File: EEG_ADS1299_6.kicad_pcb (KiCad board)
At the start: 2 copper layers, 49.6 x 21.2 mm, 90 parts, among them IC1 ADS1299, P1 CONN_2, P2 CONN_2, P3 CONN_1, P4 CONN_1, P5 CONN_01X08, P6 CONN_2, U1 TPS2294x, U2 TPS61222, U3 NRF528XX-QFAA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

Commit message: Final version, v4.
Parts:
- removed P5: CONN_01X08, Pin_Headers:Pin_Header_Straight_2x04_Pitch2.54mm
- added P10: CONN_01X02, Pin_Headers:Pin_Header_Straight_1x02_Pitch2.54mm, F.Cu at (311.0, 129.1)
- added P7: CONN_01X02, Pin_Headers:Pin_Header_Straight_1x02_Pitch2.54mm, F.Cu at (308.6, 116.0)
- added P8: CONN_01X02, Pin_Headers:Pin_Header_Straight_1x02_Pitch2.54mm, F.Cu at (311.0, 118.7)
- added P9: CONN_01X02, Pin_Headers:Pin_Header_Straight_1x02_Pitch2.54mm, F.Cu at (311.0, 123.9)
- moved P6 22.5 mm to (291.0, 116.6), turned to 90 degrees
- moved D1 17.4 mm to (273.0, 131.2)
- moved C3 16.2 mm to (270.3, 115.1), turned to 270 degrees (x2)
- moved C37 15.4 mm to (289.3, 119.0), turned to 90 degrees
- moved D2 15.3 mm to (274.2, 131.2)
- moved R14 15.0 mm to (287.4, 116.8), turned to 0 degrees
- moved R15 13.3 mm to (286.1, 117.1), turned to 270 degrees
- moved U5 13.0 mm to (287.6, 119.5), turned to 270 degrees
- moved R17 13.0 mm to (288.9, 121.6)
- moved U2 12.1 mm to (272.4, 115.3), turned to 0 degrees (x2)
- moved C13 12.1 mm to (272.5, 116.9), turned to 180 degrees (x2)
- moved R18 11.8 mm to (288.5, 123.2), turned to 270 degrees
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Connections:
- U3 pad 11: /LED2 -> /GPIO_TTDM_BAT_EN
- U3 pad 12: /LED3 -> /GPIO_ISET
- U3 pad 21: /GPIO_ISET -> Net-(U3-Pad21)
- U3 pad 22: /GPIO_TTDM_BAT_EN -> Net-(U3-Pad22)
- U3 pad 38: Net-(U3-Pad38) -> /LED3
- U3 pad 39: Net-(U3-Pad39) -> /LED2
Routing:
- net VCC: track 42.7 -> 55.5 mm, vias 2 -> 4
- net AVDD: track 67.6 -> 79.8 mm
- net /GPIO_TTDM_BAT_EN: track 18.8 -> 7.82 mm, vias 2 -> 0
- net /GPIO_ISET: track 15.6 -> 6.01 mm, vias 2 -> 0
- net /LED2: track 3.33 -> 12.8 mm
- net /LED3: track 2.56 -> 10.8 mm
- net /DC+INPUT: track 9.04 -> 2.92 mm
- net AVSS: track 196.8 -> 202.1 mm
- net /IN2-: track 6.43 -> 2.27 mm
- net DVDD: track 78.7 -> 74.8 mm, vias 8 -> 9
- net Net-(D4-Pad1): track 4.79 -> 1.51 mm
- net /IN3-: track 7.46 -> 4.27 mm
- net Net-(C4-Pad1): track 8.02 -> 5.54 mm
- net /BIASIN: track 6.27 -> 4.26 mm
- net /SRB1: track 6.16 -> 4.47 mm
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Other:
- board size 49.6 x 21.2 mm -> 46.6 x 21.2 mm
- board text added: "nRF52-ADS1299-4 with MPU & BTM ExG Prototype v4 [09/22/17] Yeo GaTech BNE Lab"
- board text removed: "nRF52-ADS1299-4 with MPU & BTM ExG Prototype v3.1 Yeo GaTech BNE Lab"

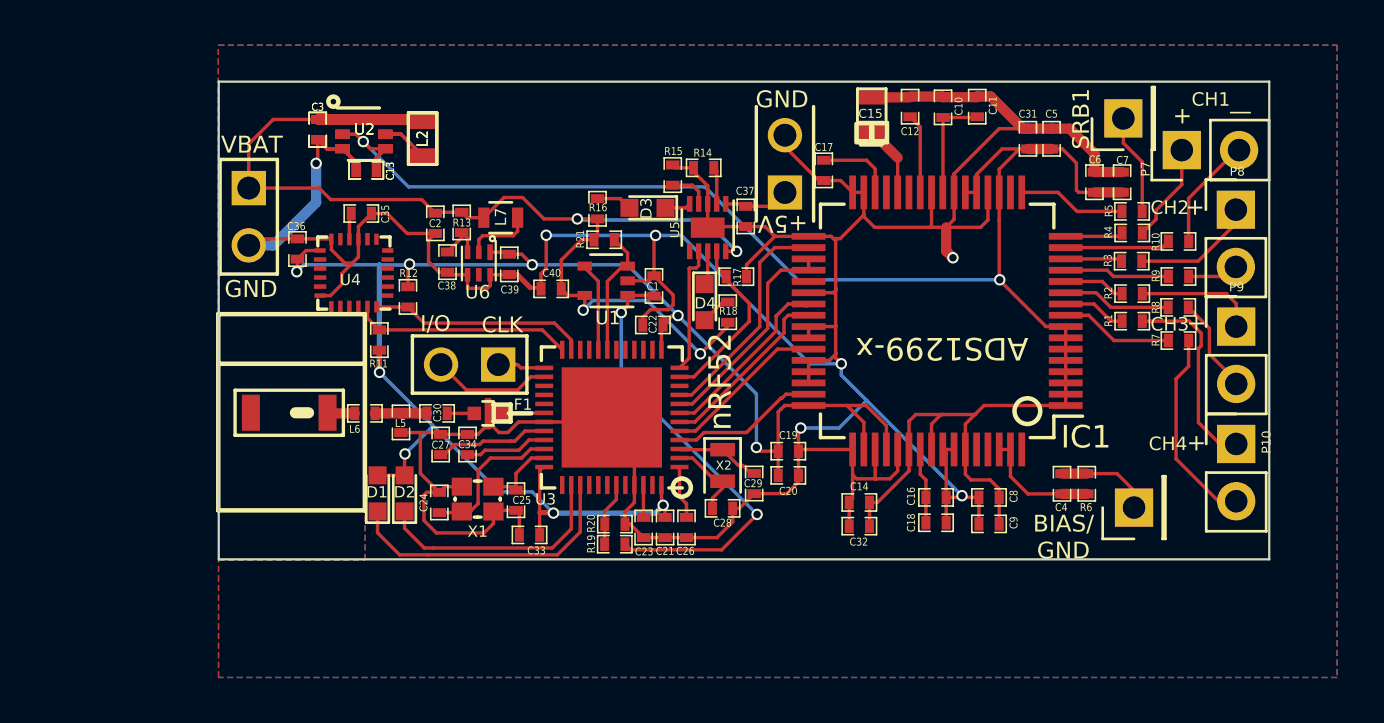
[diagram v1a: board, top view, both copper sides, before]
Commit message: Battery Management circuit. Requires revision to different ICs.
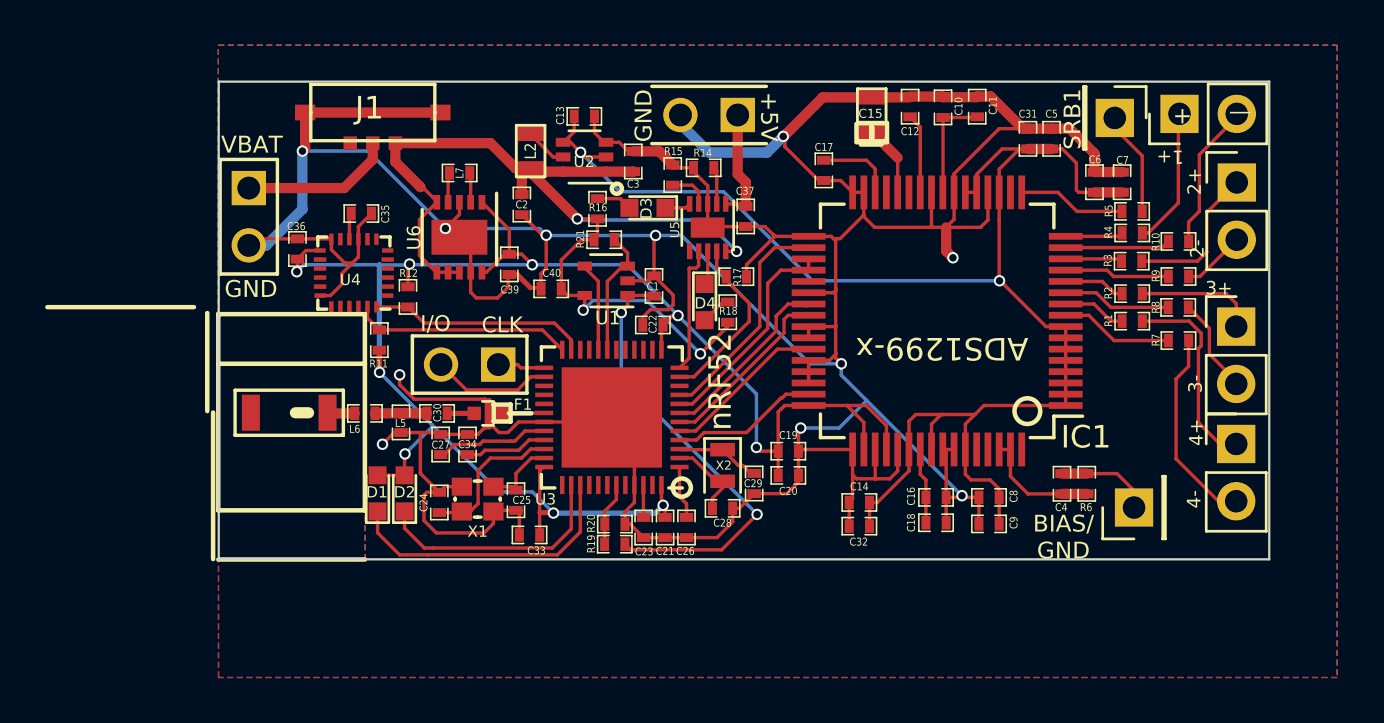
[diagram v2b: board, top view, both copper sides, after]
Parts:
- removed the C13 at (272.5, 116.9)
- removed the C3 at (270.3, 115.1)
- removed C38: 0.1uF, SM0402
- removed the L2 at (275.0, 115.5)
- removed R13: 400Ω, SM0402
- removed the U2 at (272.4, 115.3)
- added J1: CONN_01X05, Switches:SSAJ1201, F.Cu at (272.8, 114.4)
- C39: value 10uF -> 22uF
- L7: value 4.7µH -> 2.20µH; footprint Inductors_SMD:L_0603 -> SM0402
- U6: value TPS61098x -> TPS63001; footprint BGA_custom_TI:WSON_6_1.5x1.5mm -> Housings_DFN_QFN:DFN-10-1EP_3x3mm_Pitch0.5mm
- moved C3 14.1 mm to (284.3, 116.5), turned to 90 degrees
- moved C13 9.96 mm to (282.1, 114.5), turned to 0 degrees
- moved U2 9.83 mm to (282.1, 116.3), turned to 180 degrees
- moved L2 4.82 mm to (279.8, 116.1), turned to 270 degrees
- moved P6 4.00 mm to (287.7, 114.5), turned to 180 degrees
- moved C2 3.93 mm to (279.4, 118.4)
- moved L7 2.69 mm to (276.6, 117.0)
- moved P7 1.61 mm to (308.5, 114.4)
- moved U6 1.45 mm to (276.6, 119.9)
- moved P8 1.21 mm to (311.1, 117.5)
- moved P3 0.38 mm to (305.6, 114.6), turned to 270 degrees
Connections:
- C2 pad 1: VCC -> VCC_SW
- C3 pad 1: VCC -> VCC_SW
- C40 pad 1: VCC -> VCC_SW
- L2 pad 2: VCC -> VCC_SW
- L7 pad 1: VCC -> Net-(L7-Pad1)
- R16 pad 1: VCC -> VCC_SW
- R18 pad 2: VCC -> VCC_SW
- R21 pad 1: VCC -> VCC_SW
- U1 pad 5: VCC -> VCC_SW
- U2 pad 1: VCC -> VCC_SW
- U2 pad 6: VCC -> VCC_SW
- U5 pad 10: VCC -> VCC_SW
- U6 pad 3: Net-(C38-Pad1) -> AVSS
- U6 pad 4: AVSS -> Net-(L7-Pad1)
- U6 pad 5: Net-(U6-Pad5) -> VCC_SW
- U6 pad 6: AVSS -> VCC_SW
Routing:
- net VCC: track 55.5 -> 6.75 mm, vias 4 -> 0
- net VCC_SW: track 0.00 -> 47.3 mm, vias 0 -> 4
- net AVSS: track 202.1 -> 238.4 mm, vias 7 -> 11
- net AVDD: track 79.8 -> 69.0 mm
- net DVDD: track 74.8 -> 78.4 mm
- net Net-(L2-Pad1): track 4.10 -> 1.88 mm
- net /DC+INPUT: track 2.92 -> 5.12 mm
- net Net-(C38-Pad1): track 2.10 -> 0.00 mm
- net Net-(L7-Pad2): track 3.03 -> 1.32 mm
- net /IN1: track 4.40 -> 5.90 mm
- net Net-(L7-Pad1): track 0.00 -> 1.33 mm
- net /IN1-: track 5.18 -> 6.46 mm
- net /IN2: track 5.47 -> 6.68 mm
- net /IN2-: track 2.27 -> 2.81 mm
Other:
- board text added: "1+"
- board text added: "2+"
- board text added: "2-"
- board text added: "3+"
- board text added: "3-"
- board text added: "4+"
- board text added: "4-"
- board text added: "nRF52-ADS1299-4 with MPU & BTM ExG Prototype v4 [09/24/17] Yeo GaTech BNE Lab"
- board text removed: "CH1"
- board text removed: "CH2"
- board text removed: "CH3"
- board text removed: "CH4"
- board text removed: "nRF52-ADS1299-4 with MPU & BTM ExG Prototype v4 [09/22/17] Yeo GaTech BNE Lab"
